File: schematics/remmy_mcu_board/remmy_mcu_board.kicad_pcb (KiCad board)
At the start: 2 copper layers, 30 x 50 mm, 25 parts, among them J1 AVR-JTAG-10, J2 Conn_02x05_Counter_Clockwise, J3 Conn_01x03_Pin, Q1 BSS138, SW1 RotaryEncoder, SW2 SW_Push, SW3 SW_Push, SW4 SW_Push, U1 NX3225SA-16, U2 ATmega32U4-M, U3 Kailh GM 8.0, U4 Kailh GM 8.0

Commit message: added images
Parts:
- renumbered SW2 to SW1, SW1 to SW2, SW4 to SW3, SW3 to SW4, U3 to SW5, U4 to SW6, U1 to X1
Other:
- board text added: "Remmy v2.1A"
- board text removed: "Remmy v2.0A"

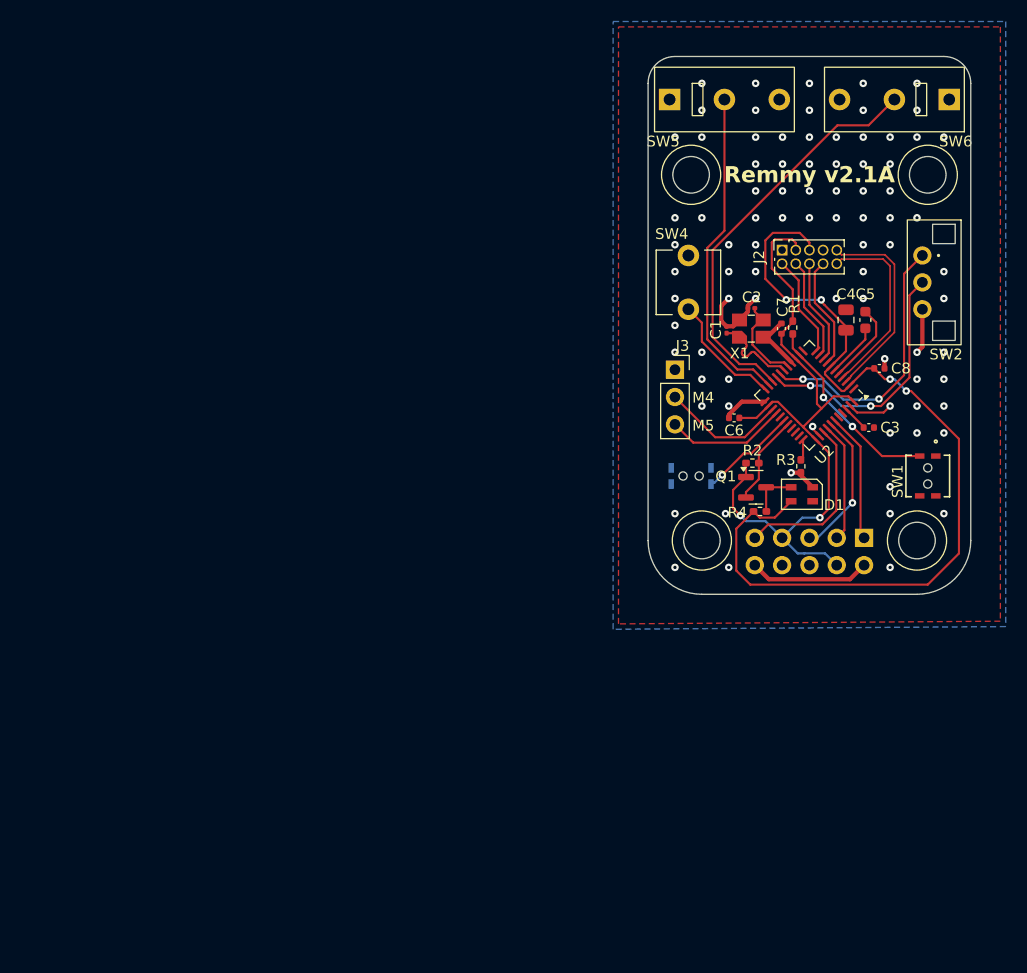
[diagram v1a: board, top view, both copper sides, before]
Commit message: broken spi comm
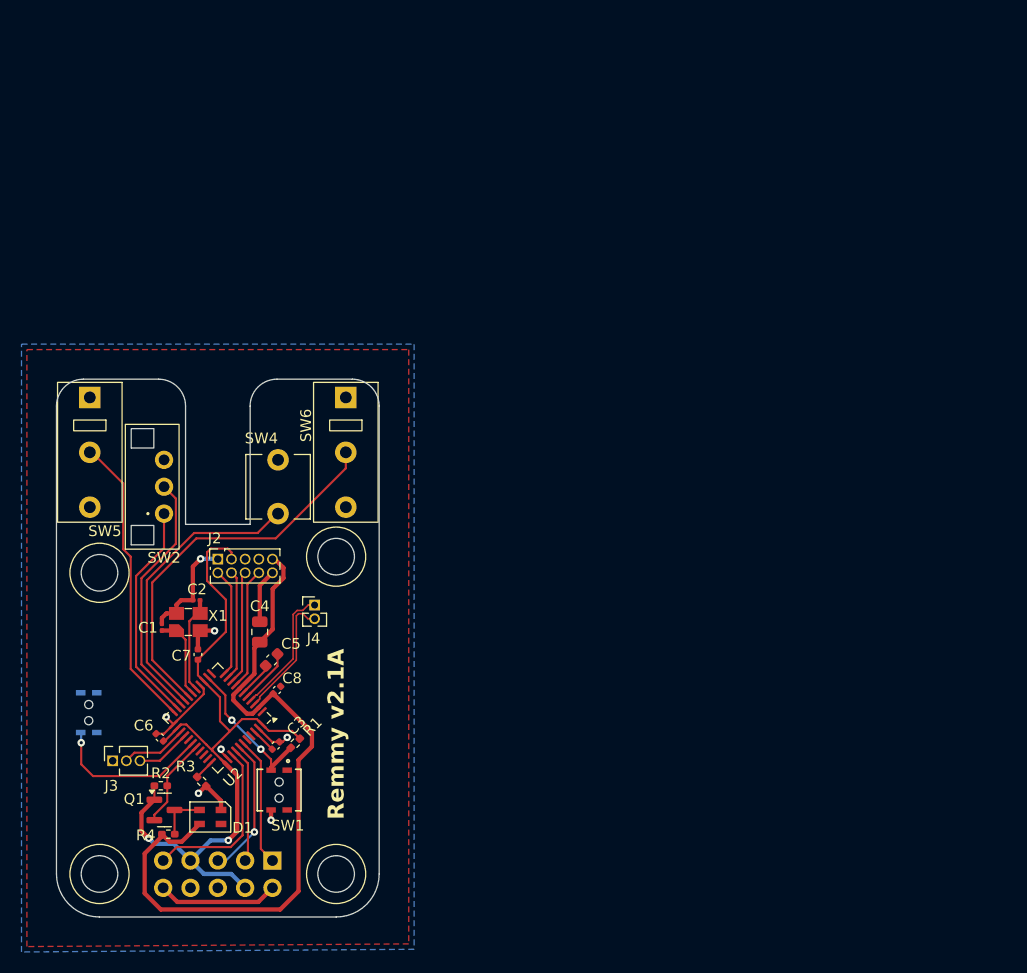
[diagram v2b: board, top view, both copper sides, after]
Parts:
- added J4: Conn_01x02, Connector_PinHeader_1.27mm:PinHeader_1x02_P1.27mm_Vertical, F.Cu at (124.0, 121.0)
- J3: footprint Connector_PinSocket_2.54mm:PinSocket_1x03_P2.54mm_Vertical -> Connector_PinSocket_1.27mm:PinSocket_1x03_P1.27mm_Vertical
- moved SW2 73.0 mm to (110.0, 110.0), turned to 90 degrees
- moved SW5 67.5 mm to (103.1, 106.8), turned to -90 degrees
- moved SW1 67.0 mm to (120.7, 138.2)
- moved J3 63.7 mm to (105.2, 135.5), turned to 90 degrees
- moved C5 63.6 mm to (120.0, 126.1), turned to 45 degrees
- moved C8 63.5 mm to (120.5, 128.9), turned to -135 degrees
- moved R3 62.9 mm to (113.5, 137.4), turned to -45 degrees
- moved Q1 62.6 mm to (110.0, 140.1)
- moved R4 62.6 mm to (110.4, 142.3)
- moved D1 62.6 mm to (114.3, 140.7)
- moved R2 62.6 mm to (109.7, 137.8)
- moved U2 62.6 mm to (115.0, 131.5)
- moved J1 62.6 mm to (120.1, 144.8)
- moved C3 62.6 mm to (120.4, 134.1), turned to -135 degrees
- moved C7 62.1 mm to (113.2, 125.6)
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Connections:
- C3 pad 1: Net-(U2-AREF) -> GND
- C3 pad 2: GND -> Net-(U2-AREF)
- C4 pad 1: GND -> +5V
- C4 pad 2: +5V -> GND
- J2 pad 3: +5V -> GND
- J2 pad 5: D- -> +5V
- J2 pad 6: D+ -> GND
- U2 pad 18: ENCODER_A -> MOUSE2
- U2 pad 19: ENCODER_B -> MWHEEL_BUTTON
- U2 pad 20: MOUSE2 -> ENCODER_B
- U2 pad 21: MOUSE1 -> ENCODER_A
- U2 pad 22: MWHEEL_BUTTON -> MOUSE1
- U2 pad 3: D- -> Net-(J4-Pin_2)
- U2 pad 4: D+ -> Net-(J4-Pin_1)
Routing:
- net D-: track 18.7 -> 0.00 mm
- net D+: track 17.7 -> 0.00 mm
- net +5V: track 84.0 -> 67.2 mm, vias 4 -> 0
- net MWHEEL_BUTTON: track 11.2 -> 27.4 mm
- net Net-(J4-Pin_1): track 0.00 -> 12.1 mm
- net Net-(J4-Pin_2): track 0.00 -> 11.8 mm
- net MOUSE5: track 11.3 -> 5.13 mm
- net DPI: track 9.27 -> 15.0 mm
- net MOUSE4: track 11.7 -> 6.19 mm
- net ENCODER_A: track 25.3 -> 20.7 mm, vias 2 -> 0
- net Net-(U2-~{RESET}): track 18.3 -> 13.9 mm
- net +3.3V: track 65.6 -> 69.7 mm
- net MOUSE1: track 30.5 -> 27.5 mm
- net GND: track 49.5 -> 52.3 mm, vias 85 -> 7
- net MOUSE2: track 38.1 -> 35.9 mm
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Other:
- outline, holes or cut-outs redrawn
- board text removed: "M4"
- board text removed: "M5"
